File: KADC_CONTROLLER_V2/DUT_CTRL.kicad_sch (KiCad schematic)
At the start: 2 parts, among them J2 QSH-040-01-X-D-DP-A, J4 QSH-040-01-X-D-DP-A

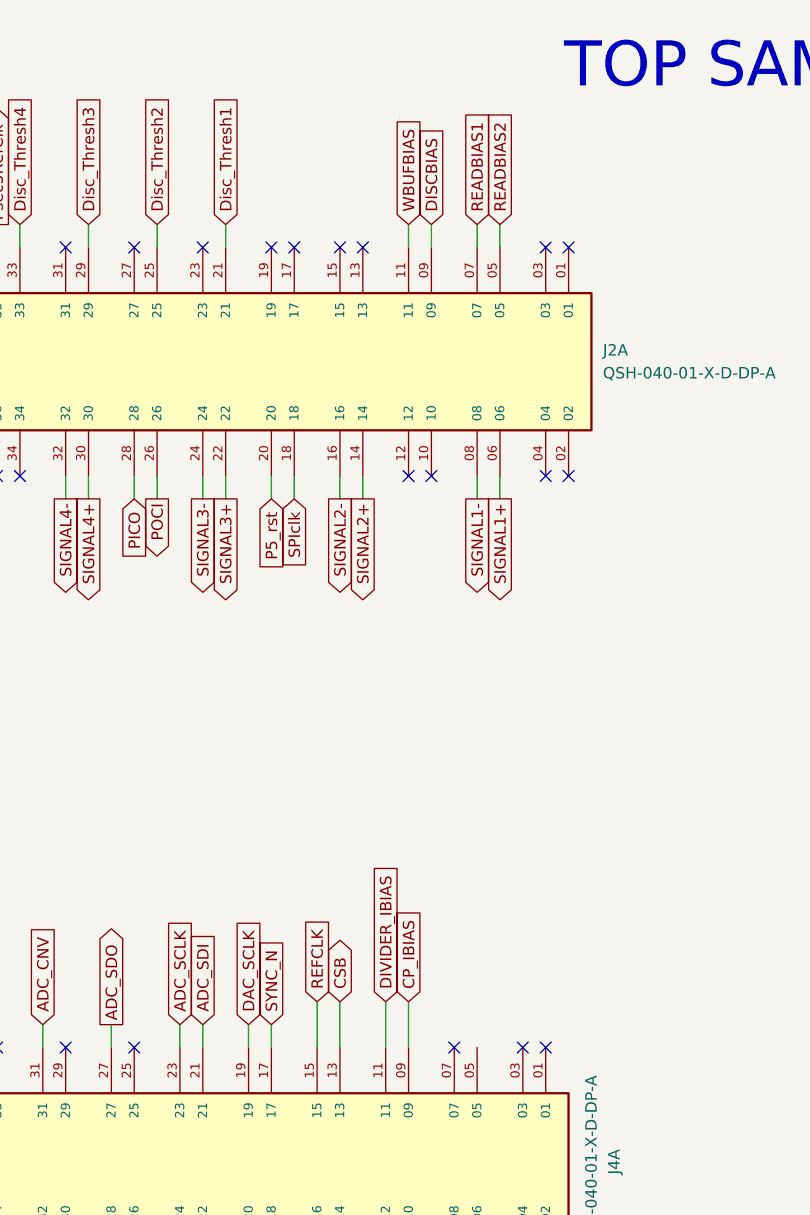
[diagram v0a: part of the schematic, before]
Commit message: Updates SD card on KADC
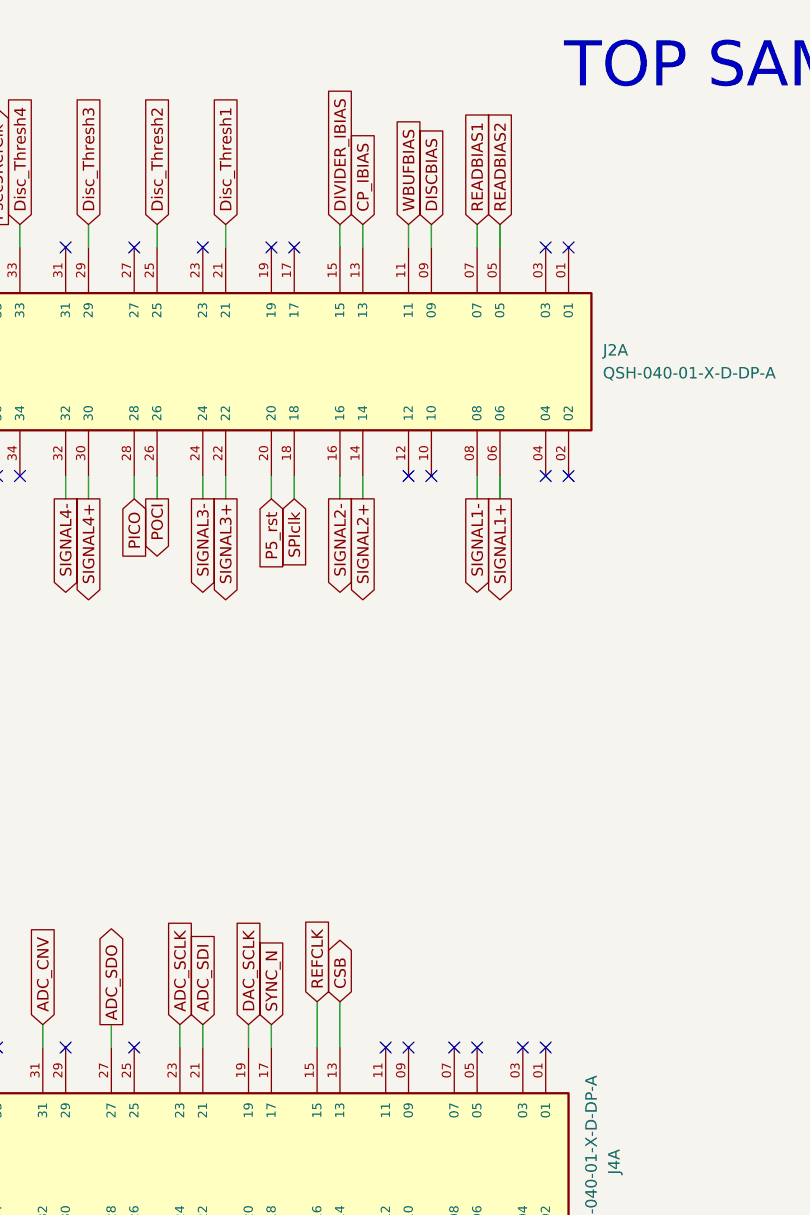
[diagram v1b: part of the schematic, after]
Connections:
- net CP_IBIAS: now also J2.13; no longer J4.09
- net DIVIDER_IBIAS: now also J2.15; no longer J4.11
- no-connect marks 67 -> 68
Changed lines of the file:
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@@
 	)
 	(no_connect
-		(at 219.71 34.29)
-	)
-	(no_connect
 		(at 229.87 59.69)
 	)
@@
 	)
 	(no_connect
-		(at 222.25 34.29)
-	)
-	(no_connect
 		(at 76.2 35.56)
 	)
@@
 	)
 	(no_connect
+		(at 224.79 123.19)
+	)
+	(no_connect
 		(at 227.33 59.69)
 	)
@@
 	)
 	(no_connect
+		(at 227.33 123.19)
+	)
+	(no_connect
 		(at 133.35 147.32)
 	)
@@
 	)
 	(no_connect
+		(at 234.95 123.19)
+	)
+	(no_connect
 		(at 189.23 123.19)
 	)
@@
 	(wire
 		(pts
+			(xy 219.71 31.75) (xy 219.71 34.29)
+		)
+		(stroke
+			(width 0)
+			(type default)
+		)
+	)
+	(wire
+		(pts
 			(xy 92.71 149.86) (xy 95.25 149.86)
 		)
@@
 	(wire
 		(pts
+			(xy 222.25 31.75) (xy 222.25 34.29)
+		)
+		(stroke
+			(width 0)
+			(type default)
+		)
+	)
+	(wire
+		(pts
 			(xy 209.55 148.59) (xy 209.55 151.13)
 		)
@@
 	(wire
 		(pts
-			(xy 227.33 118.11) (xy 227.33 123.19)
-		)
-		(stroke
-			(width 0)
-			(type default)
-		)
-	)
-	(wire
-		(pts
 			(xy 77.47 151.13) (xy 77.47 153.67)
 		)
@@
 	(wire
 		(pts
-			(xy 224.79 118.11) (xy 224.79 123.19)
-		)
-		(stroke
-			(width 0)
-			(type default)
-		)
-	)
-	(wire
-		(pts
 			(xy 214.63 59.69) (xy 214.63 62.23)
 		)
@@
 	(global_label "CP_IBIAS"
 		(shape input)
-		(at 227.33 118.11 90)
+		(at 222.25 31.75 90)
 		(fields_autoplaced yes)
 		(effects
@@
 		)
 		(property "Intersheetrefs" "${INTERSHEET_REFS}"
-			(at 227.33 106.8395 90)
+			(at 222.25 20.4795 90)
 			(hide yes)
 			(show_name no)
@@
 	(global_label "DIVIDER_IBIAS"
 		(shape input)
-		(at 224.79 118.11 90)
+		(at 219.71 31.75 90)
 		(fields_autoplaced yes)
 		(effects
@@
 		)
 		(property "Intersheetrefs" "${INTERSHEET_REFS}"
-			(at 224.79 102.1223 90)
+			(at 219.71 15.7623 90)
 			(hide yes)
 			(show_name no)

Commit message: Quick Updates
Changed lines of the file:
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@@
 	)
 	(global_label "CSB"
-		(shape bidirectional)
+		(shape input)
 		(at 219.71 118.11 90)
 		(fields_autoplaced yes)
@@
 		)
 		(property "Intersheetrefs" "${INTERSHEET_REFS}"
-			(at 219.71 110.264 90)
+			(at 219.71 111.3753 90)
 			(hide yes)
 			(show_name no)
